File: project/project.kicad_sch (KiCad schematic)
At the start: 0 parts

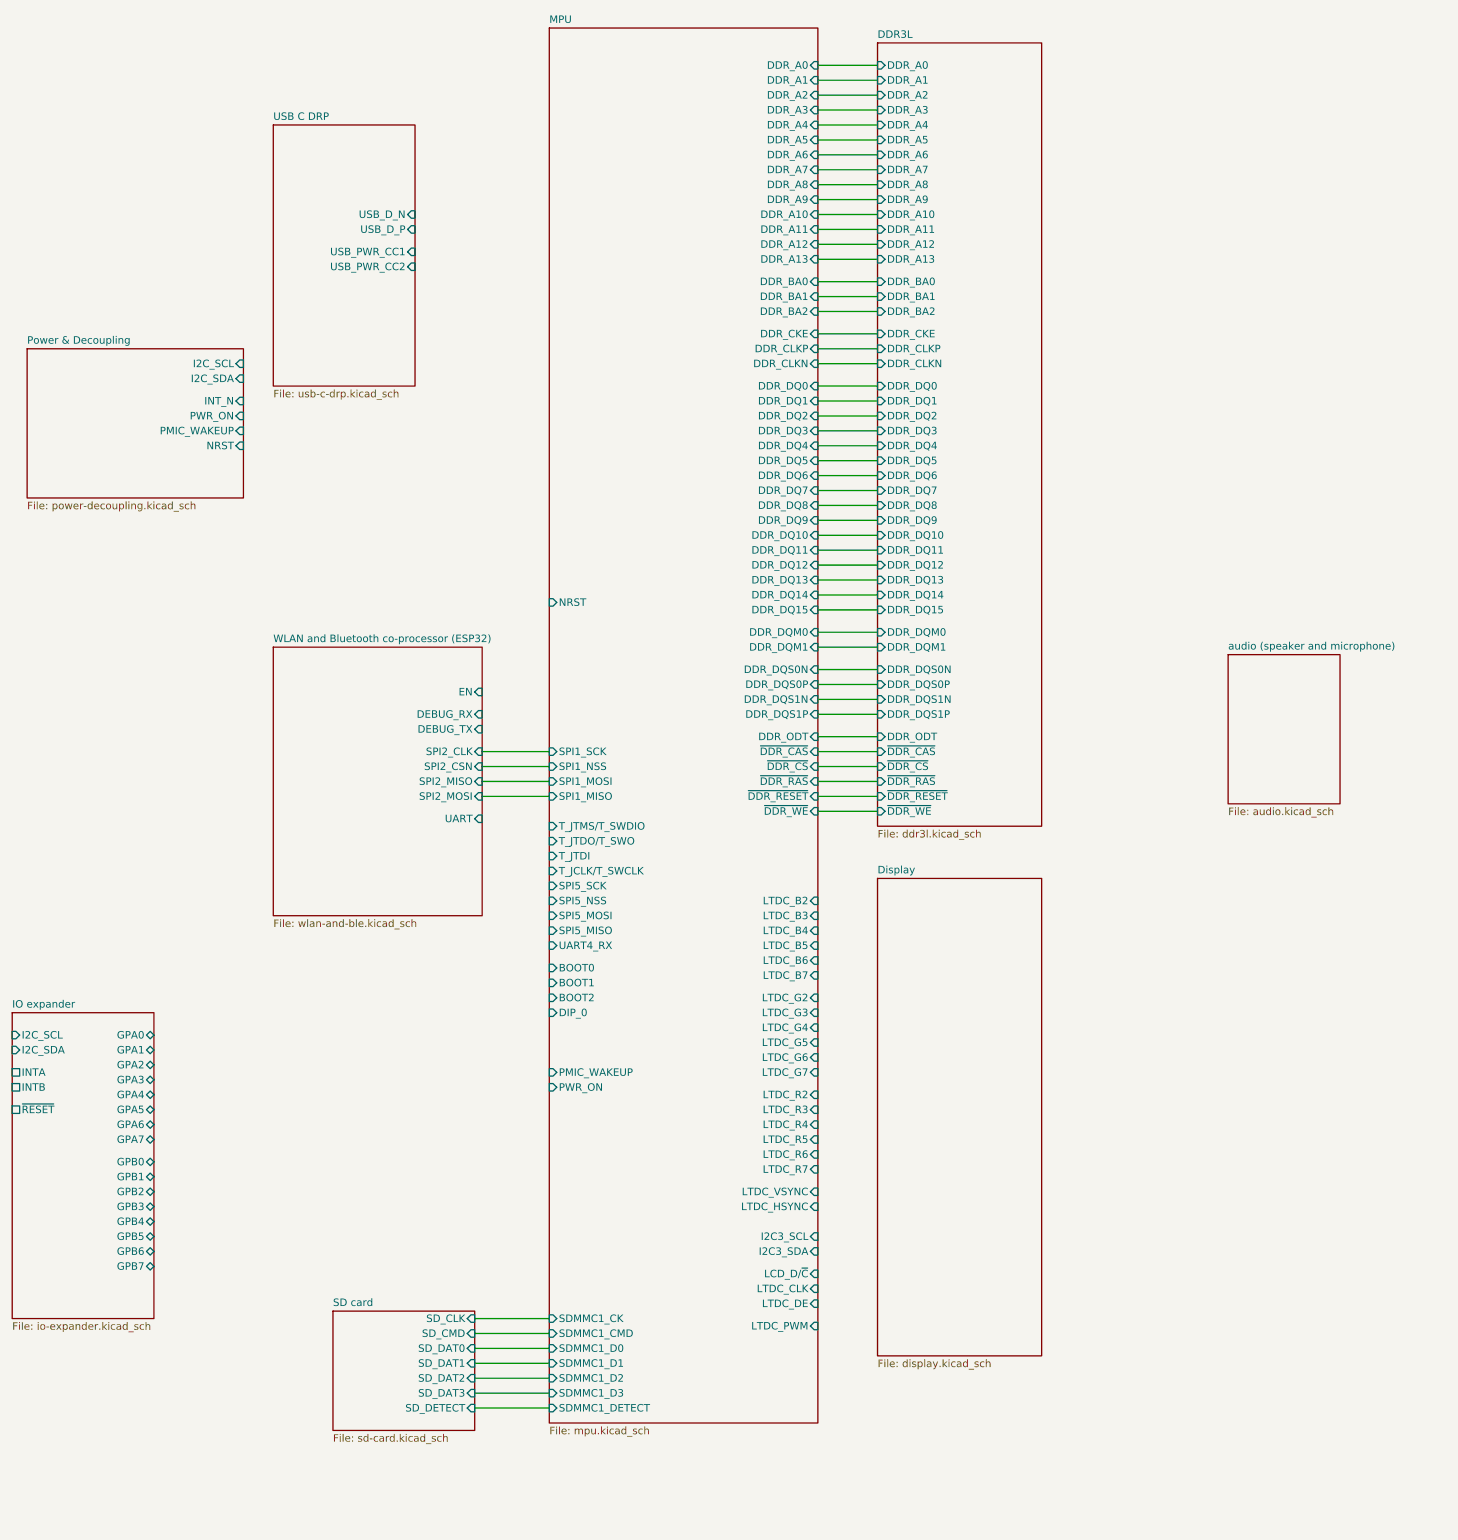
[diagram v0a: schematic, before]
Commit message: Minor changes to audio design
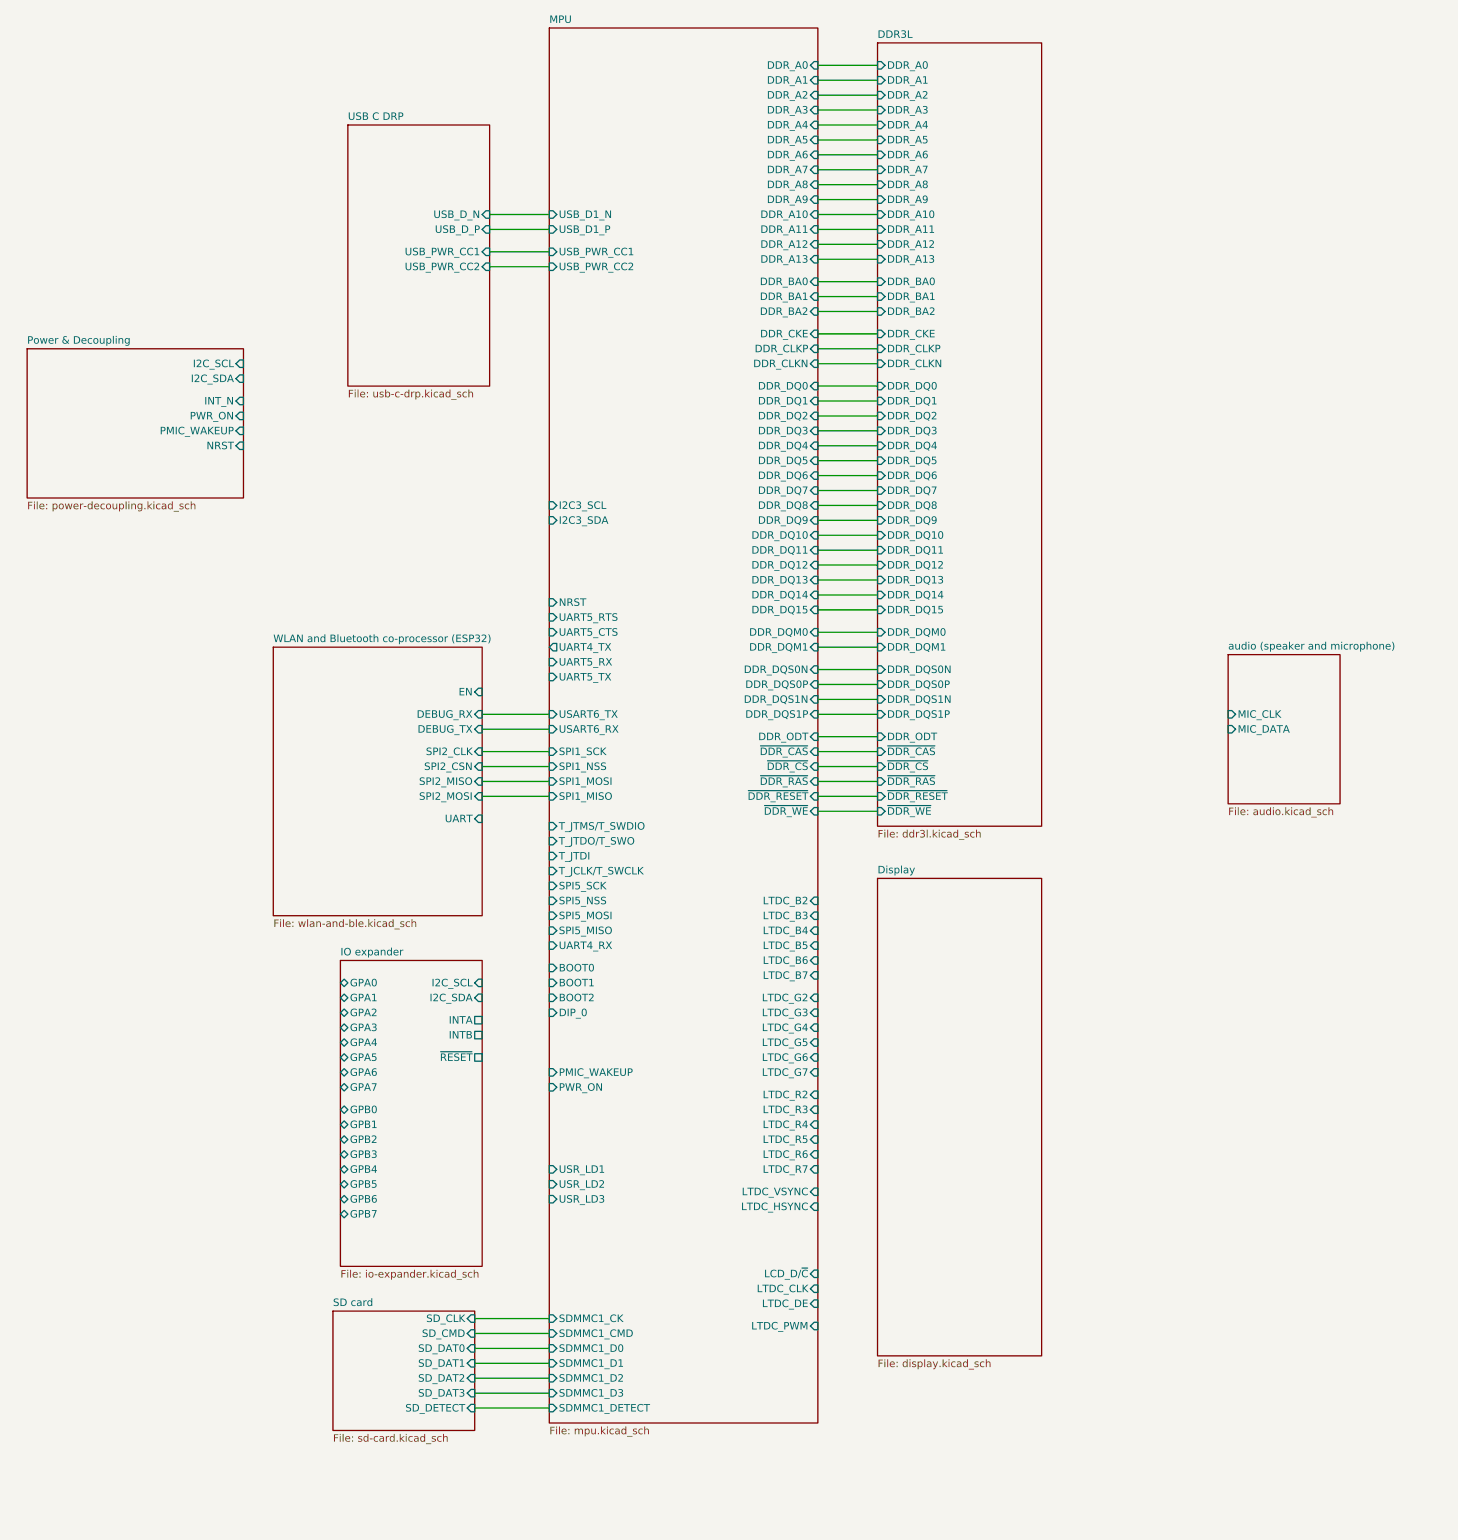
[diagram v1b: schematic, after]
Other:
- sheet MPU ports: added UART4_TX, UART5_CTS, UART5_RTS, UART5_RX, UART5_TX, USART6_RX, USART6_TX, USB_D1_N, USB_D1_P, USB_PWR_CC1, USB_PWR_CC2, USR_LD1, USR_LD2, USR_LD3; removed none
- sheet audio (speaker and microphone) ports: added MIC_CLK, MIC_DATA; removed none

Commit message: schemtic is done, need to go through BOM
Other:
- sheet IO expander renamed GPIO & IO expander
- added sheet Keypad (keypad.kicad_sch)
- sheet Display ports: added LCD_CSX, LCD_DAT0, LCD_DAT1, LCD_DAT2, LCD_DAT3, LCD_DAT4, LCD_DAT5, LCD_DAT6, LCD_DAT7, LCD_D/CX, LCD_RDX, LCD_RESX, LCD_TE, LCD_WRX; removed none
- sheet GPIO & IO expander ports: added BOOT0, BOOT1, BOOT2, IO_EX_I2C_SCL, IO_EX_I2C_SDA, IO_EX_INT, NRST, T_JCLK/T_SWCLK, T_JTDI, T_JTDO/T_SWO, T_JTMS/T_SWDIO, T_VCP_RX, T_VCP_TX, UART_CTS, UART_RTS, UART_RX, UART_TX; removed GPA6, GPA7, GPB6, GPB7, I2C_SCL, I2C_SDA, INTA, INTB, ~{RESET}
- sheet MPU ports: added BFG_GPIO0, DISPLAY_GPIO0, DISPLAY_GPIO1, FMC_A3, FMC_D0, FMC_D1, FMC_D2, FMC_D3, FMC_D4, FMC_D5, FMC_D6, FMC_D7, FMC_NE3, FMC_NOE, FMC_NWE, I2C4_SCL, I2C4_SDA, IO_EX_GPIO0, PMIC_GPIO0, PMIC_GPIO1, SAI1_CK1, SAI1_D1, SAI2_FS_B, SAI2_SCK_B, SAI2_SD_A, SAI2_SD_B, USART2_CTS, USART2_RTS, USART2_RX, USART2_TX, USB_PWR_GPIO0, USB_PWR_GPIO1, VSOURCE_GPIO0, WIFI_BLE_GPIO0; removed DIP_0, LCD_D/~{C}, LTDC_B2, LTDC_B3, LTDC_B4, LTDC_B5, LTDC_B6, LTDC_B7, LTDC_CLK, LTDC_DE, LTDC_G2, LTDC_G3, LTDC_G4, LTDC_G5, LTDC_G6, LTDC_G7, LTDC_HSYNC, LTDC_PWM, LTDC_R2, LTDC_R3, LTDC_R4, LTDC_R5, LTDC_R6, LTDC_R7, LTDC_VSYNC, PMIC_WAKEUP, SPI5_MISO, SPI5_MOSI, SPI5_NSS, SPI5_SCK, UART5_CTS, UART5_RTS, USART6_RX, USART6_TX, USB_PWR_CC1, USB_PWR_CC2, USR_LD1, USR_LD2, USR_LD3
- sheet Power & Decoupling ports: added PMIC_INT_N; removed INT_N
- sheet USB C DRP ports: added BFG_ALRT, BFG_SCL, BFG_SDA, VSOURCE_IO; removed none
- sheet WLAN and Bluetooth co-processor (ESP32) ports: added none; removed UART
- sheet audio (speaker and microphone) ports: added I2C_SCL, I2C_SDA, I2S_BCLK, I2S_SDI, I2S_SDO, I2S_WCLK, NRST; removed none
- note added: "Assuming that SDO is data output (ADC) then connect to SAI_SD_A (input) Assuming that SDI is data input (DAC) then connect to SAI_SD_B (output)"

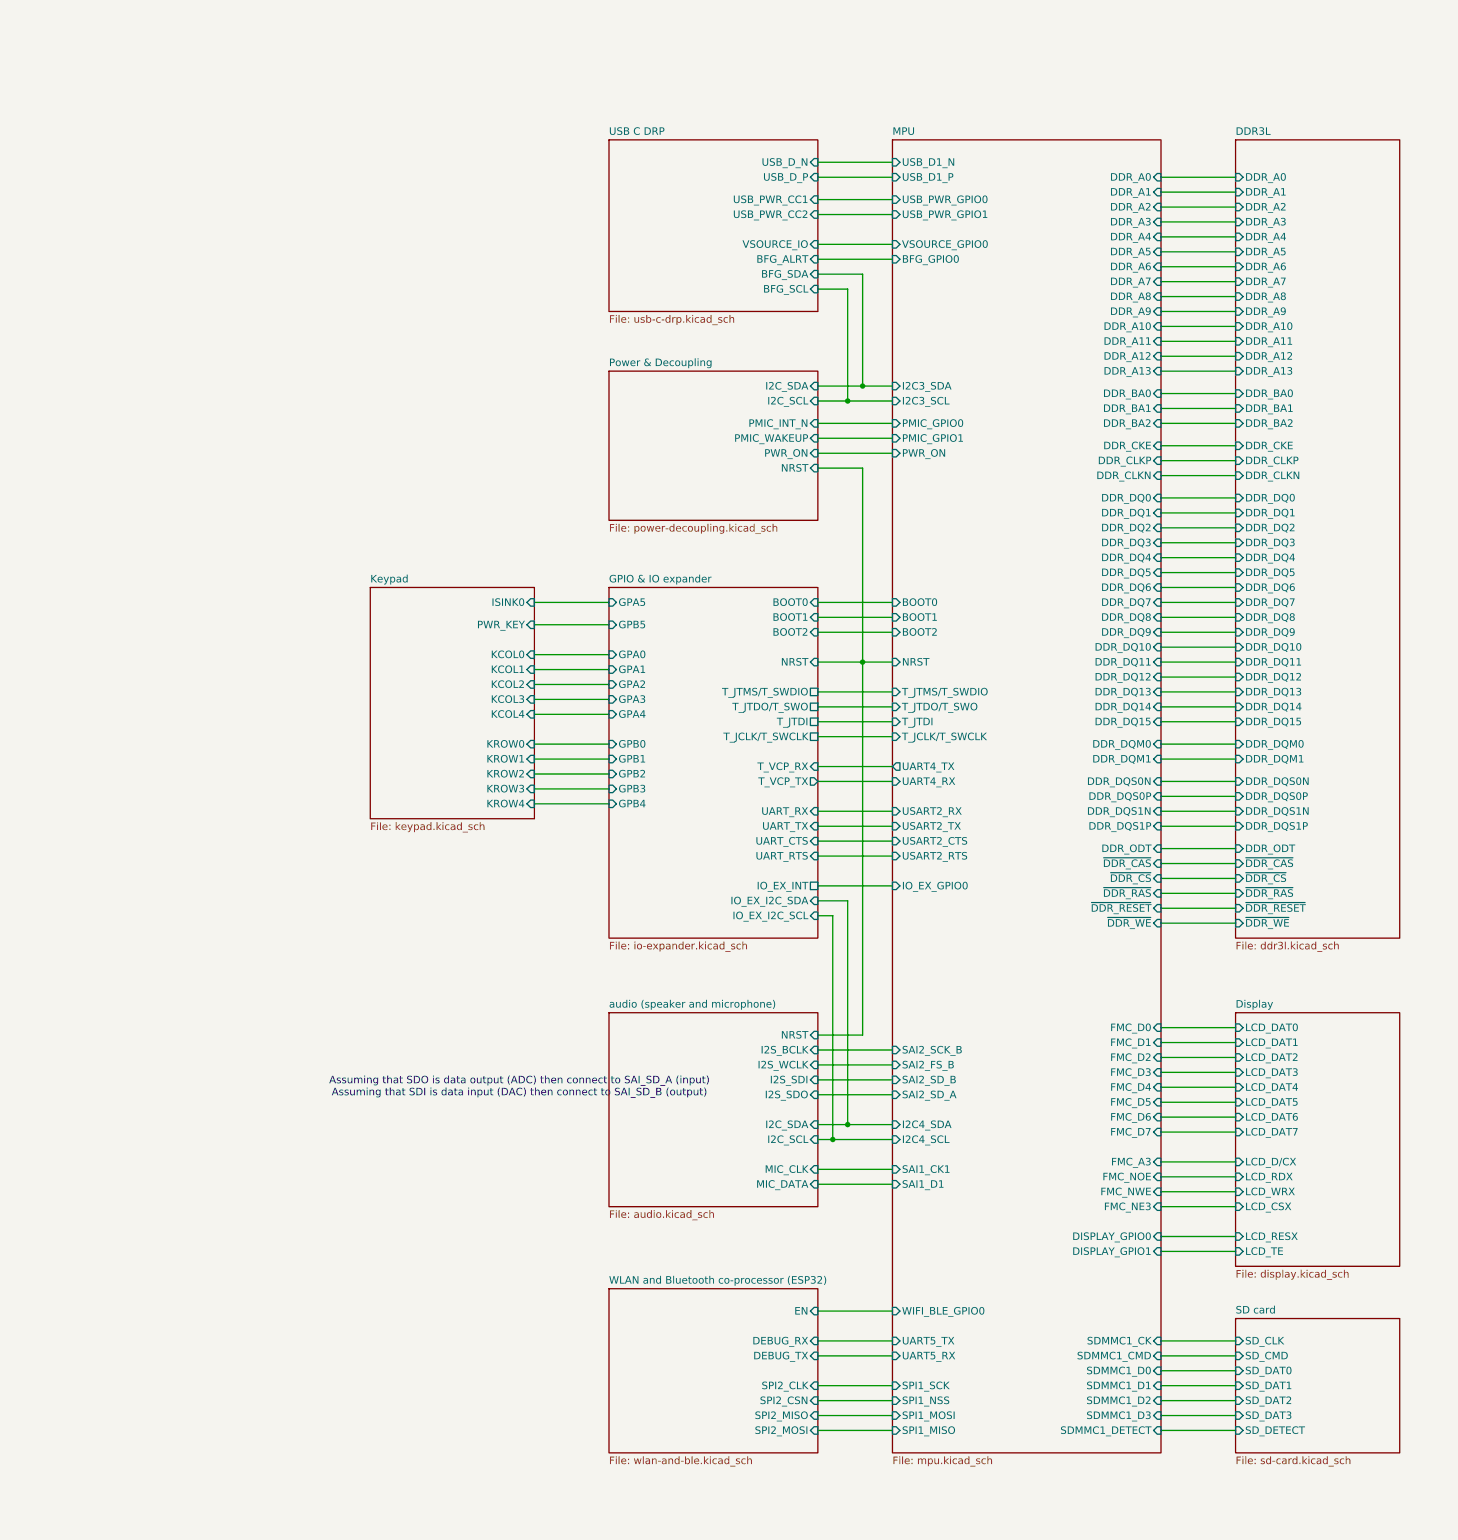
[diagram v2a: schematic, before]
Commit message: schemtic is done, annotation set
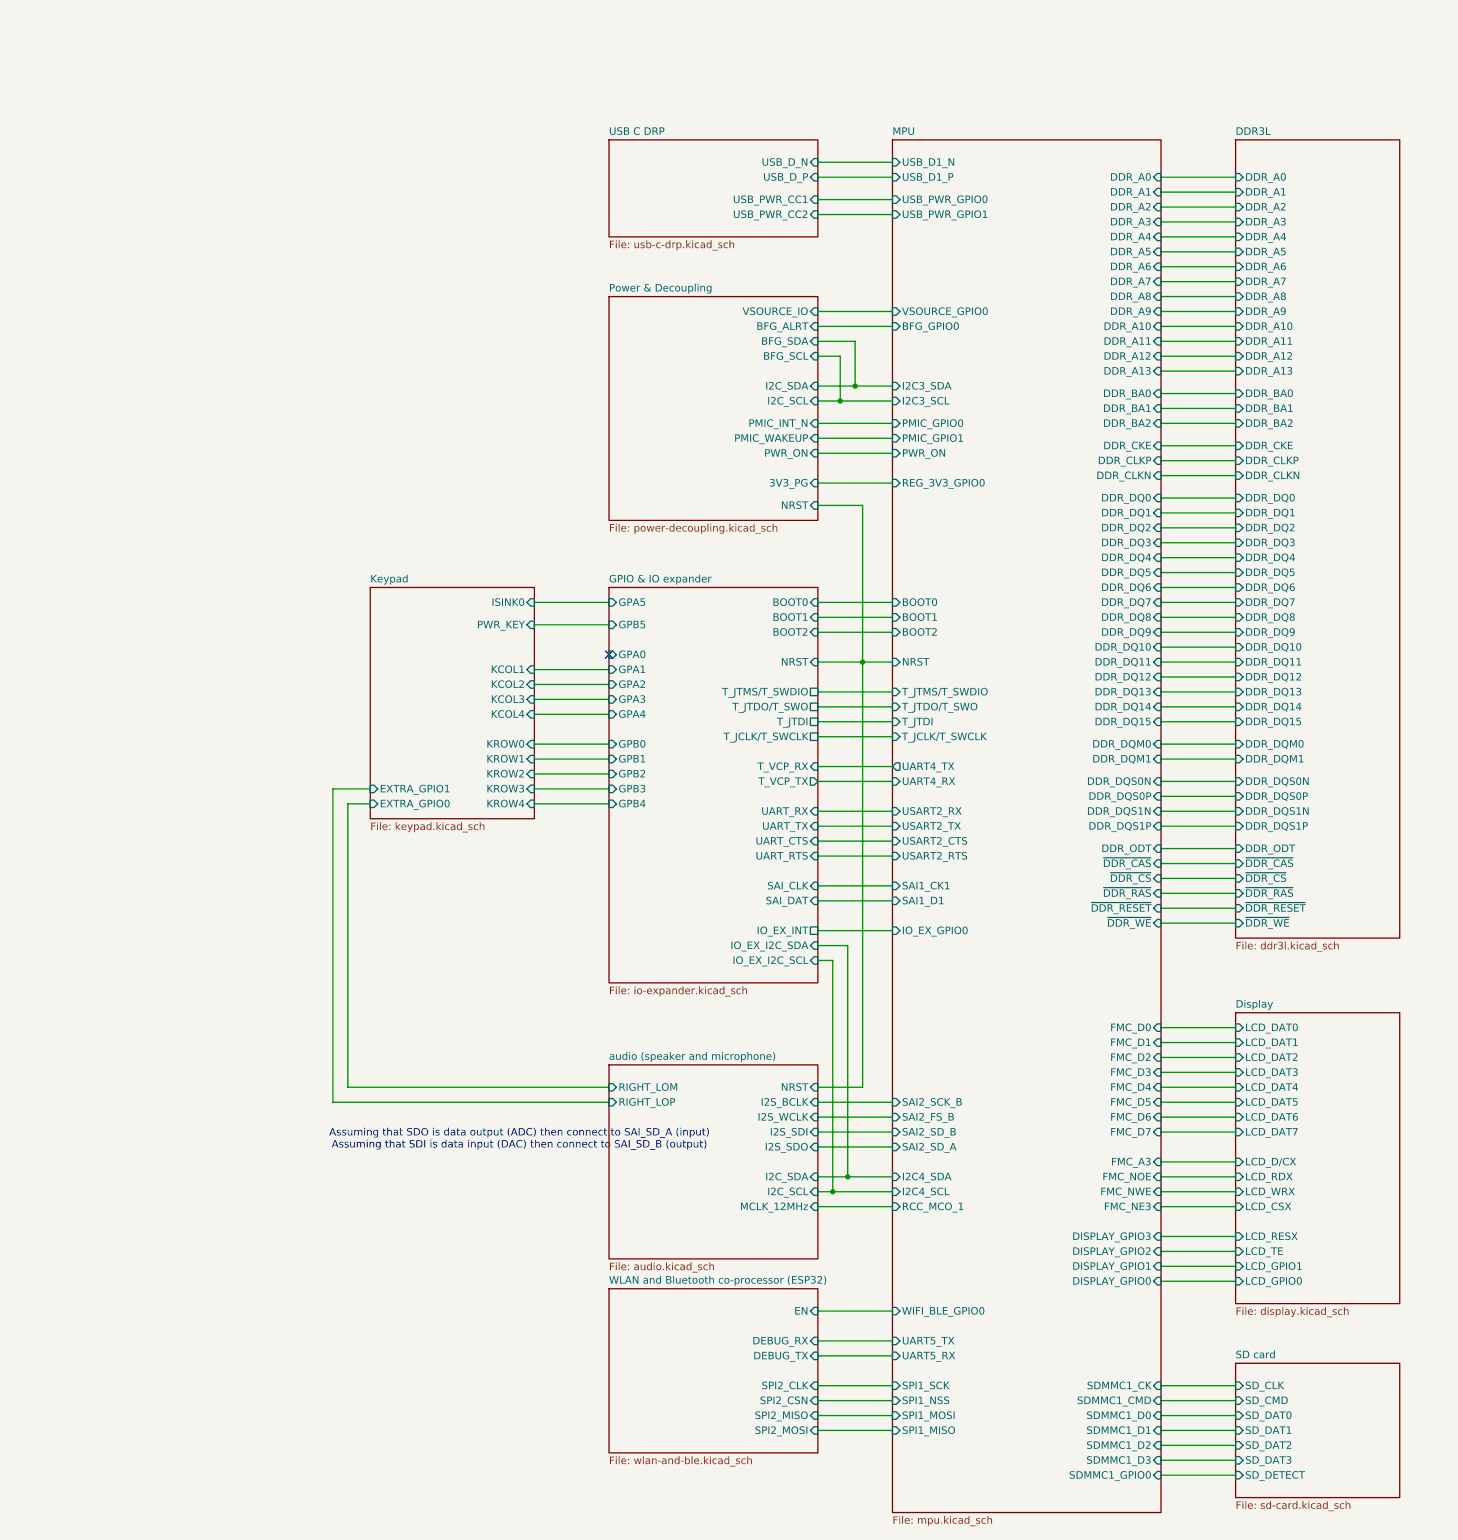
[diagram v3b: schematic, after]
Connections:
- no-connect marks 0 -> 1
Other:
- sheet Display ports: added LCD_GPIO0, LCD_GPIO1; removed none
- sheet GPIO & IO expander ports: added SAI_CLK, SAI_DAT; removed none
- sheet Keypad ports: added EXTRA_GPIO0, EXTRA_GPIO1; removed KCOL0
- sheet MPU ports: added DISPLAY_GPIO2, DISPLAY_GPIO3, RCC_MCO_1, REG_3V3_GPIO0, SDMMC1_GPIO0; removed SDMMC1_DETECT
- sheet Power & Decoupling ports: added 3V3_PG, BFG_ALRT, BFG_SCL, BFG_SDA, VSOURCE_IO; removed none
- sheet USB C DRP ports: added none; removed BFG_ALRT, BFG_SCL, BFG_SDA, VSOURCE_IO
- sheet audio (speaker and microphone) ports: added MCLK_12MHz, RIGHT_LOM, RIGHT_LOP; removed MIC_CLK, MIC_DATA
